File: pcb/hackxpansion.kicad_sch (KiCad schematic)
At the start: 0 parts

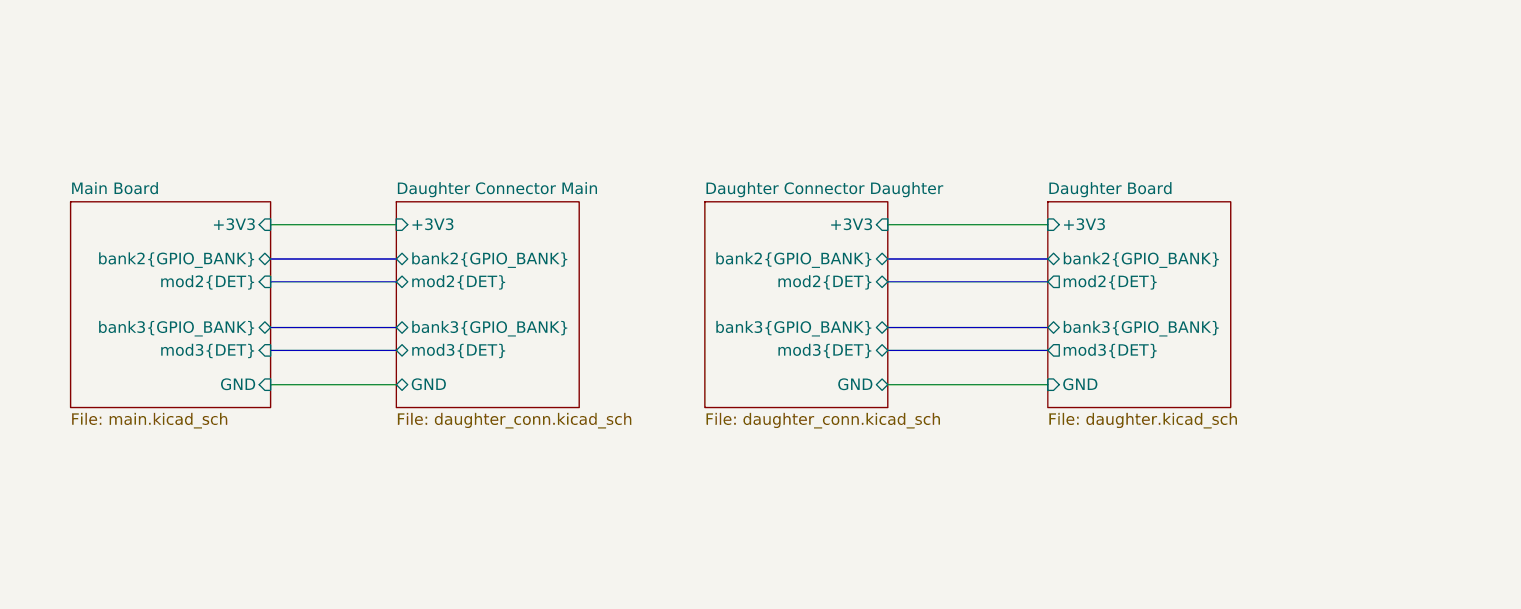
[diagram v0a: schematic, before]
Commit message: finished rough schematic
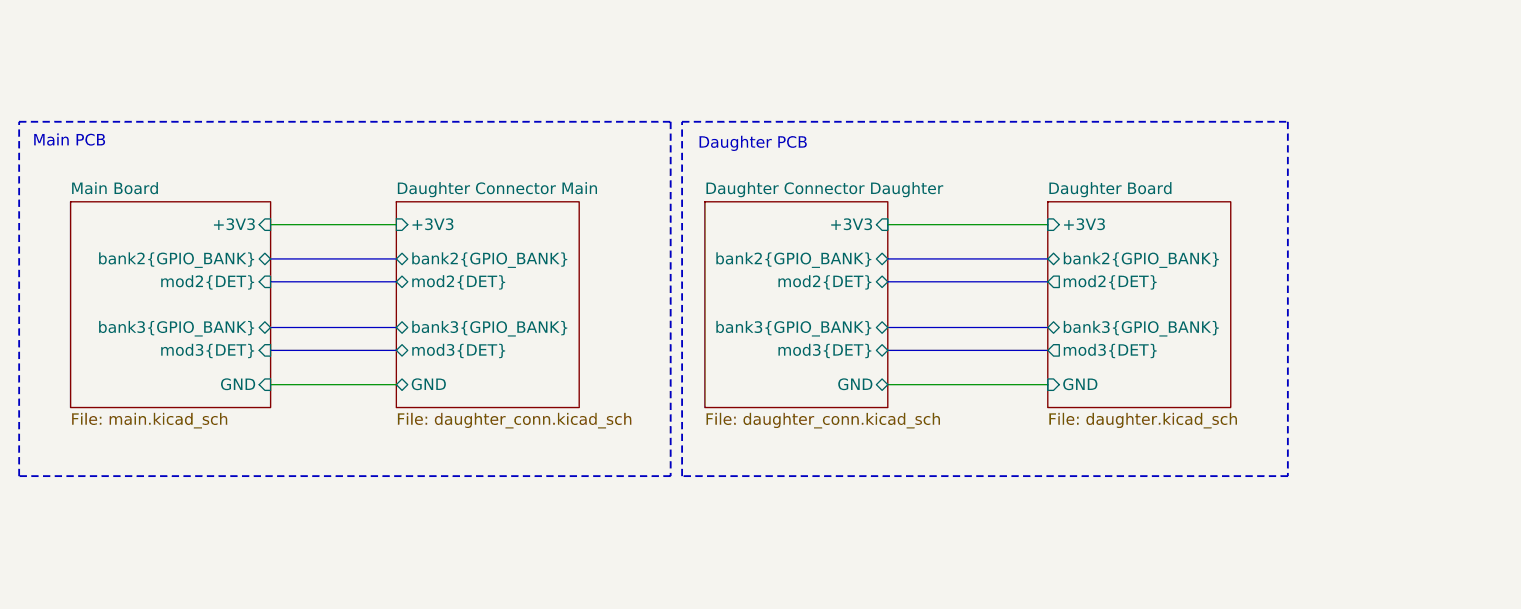
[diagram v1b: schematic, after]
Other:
- note added: "Daughter PCB"
- note added: "Main PCB"
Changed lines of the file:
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@@
 	(generator_version "10.0")
 	(paper "A5")
+	(rectangle
+		(start 26.67 45.72)
+		(end 99.06 85.09)
+		(stroke
+			(width 0.2032)
+			(type dash)
+		)
+		(fill
+			(type none)
+		)
+	)
+	(rectangle
+		(start 100.33 45.72)
+		(end 167.64 85.09)
+		(stroke
+			(width 0.2032)
+			(type dash)
+		)
+		(fill
+			(type none)
+		)
+	)
+	(text "Main PCB"
+		(exclude_from_sim no)
+		(at 32.258 48.006 0)
+		(effects
+			(font
+				(size 1.27 1.27)
+			)
+		)
+	)
+	(text "Daughter PCB"
+		(exclude_from_sim no)
+		(at 108.204 48.26 0)
+		(effects
+			(font
+				(size 1.27 1.27)
+			)
+		)
+	)
 	(bus
 		(pts

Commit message: switched to pico blade connectors
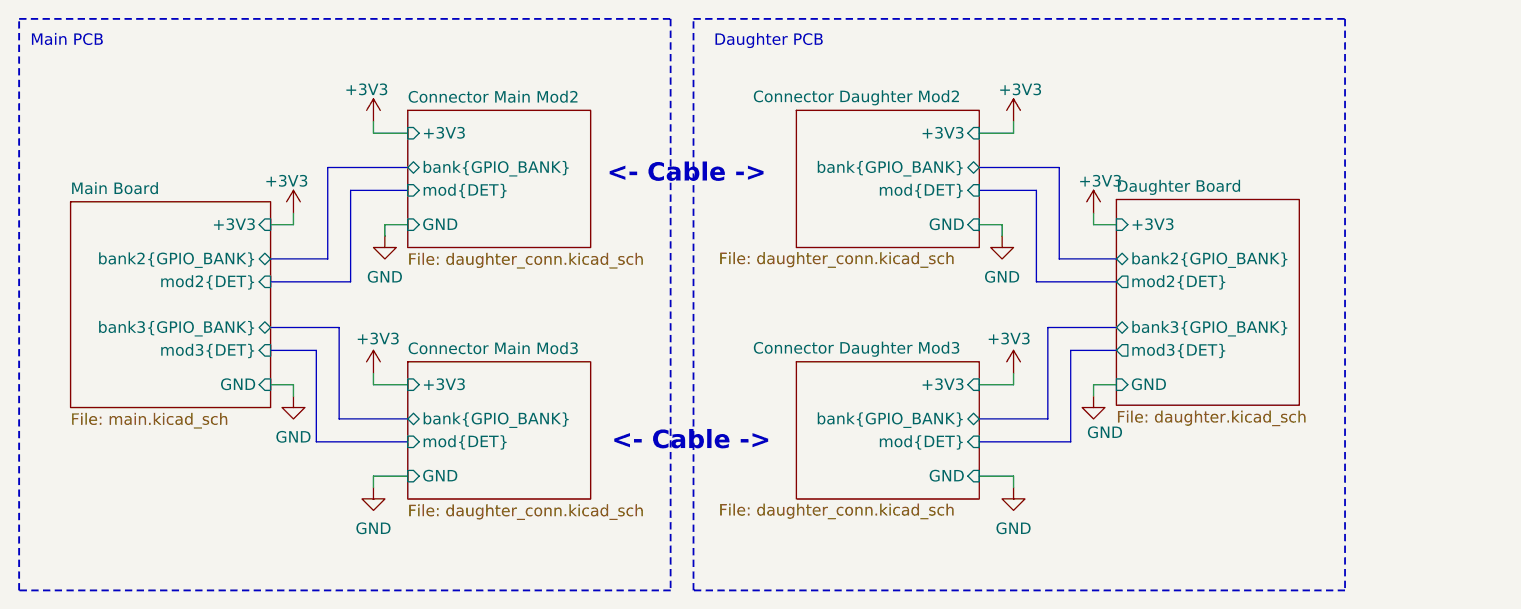
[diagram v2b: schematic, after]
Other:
- sheet Daughter Connector Main renamed Connector Main Mod2
- removed sheet Daughter Connector Daughter
- added sheet Connector Daughter Mod2 (daughter_conn.kicad_sch)
- added sheet Connector Daughter Mod3 (daughter_conn.kicad_sch)
- added sheet Connector Main Mod3 (daughter_conn.kicad_sch)
- sheet Connector Main Mod2 ports: added bank{GPIO_BANK}, mod{DET}; removed bank2{GPIO_BANK}, bank3{GPIO_BANK}, mod2{DET}, mod3{DET}
- note added: "<- Cable ->"

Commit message: moved stuff around
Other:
- note added: "<----Cable---->"
- note removed: "<- Cable ->"

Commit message: worked on routing
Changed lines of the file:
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@@
 	(wire
 		(pts
-			(xy 160.02 55.88) (xy 160.02 57.15)
+			(xy 160.02 52.07) (xy 160.02 57.15)
 		)
 		(stroke
@@
 			)
 		)
-		(property "Value" "+3V3"
+		(property "Value" "DAUGHT_+3V3"
 			(at 150.622 69.85 0)
 			(show_name no)
@@
 			)
 		)
-		(property "Value" "MAIN_GND"
+		(property "Value" "GND"
 			(at 57.15 90.932 0)
 			(show_name no)
@@
 			)
 		)
-		(property "Value" "+3V3"
-			(at 151.892 42.164 0)
+		(property "Value" "DAUGHT_+3V3"
+			(at 160.782 43.942 0)
 			(show_name no)
 			(do_not_autoplace no)
@@
 			)
 		)
-		(property "Value" "MAIN_GND"
+		(property "Value" "GND"
 			(at 67.31 65.532 0)
 			(show_name no)
@@
 		(lib_name "+3V3_1")
 		(lib_id "power:+3V3")
-		(at 160.02 55.88 0)
+		(at 160.02 52.07 0)
 		(mirror y)
 		(unit 1)
@@
 		(dnp no)
 		(property "Reference" "#PWR096"
-			(at 160.02 59.69 0)
-			(hide yes)
-			(show_name no)
-			(do_not_autoplace no)
-			(effects
-				(font
-					(size 1.27 1.27)
-				)
-			)
-		)
-		(property "Value" "+3V3"
-			(at 160.274 52.578 0)
+			(at 160.02 55.88 0)
+			(hide yes)
+			(show_name no)
+			(do_not_autoplace no)
+			(effects
+				(font
+					(size 1.27 1.27)
+				)
+			)
+		)
+		(property "Value" "DAUGHT_+3V3"
+			(at 169.164 50.038 0)
 			(show_name no)
 			(do_not_autoplace no)
@@
 		)
 		(property "Footprint" ""
-			(at 160.02 55.88 0)
+			(at 160.02 52.07 0)
 			(hide yes)
 			(show_name no)
@@
 		)
 		(property "Datasheet" ""
-			(at 160.02 55.88 0)
+			(at 160.02 52.07 0)
 			(hide yes)
 			(show_name no)
@@
 		)
 		(property "Description" "Power symbol creates a global label with name \"+3V3\""
-			(at 160.02 55.88 0)
-			(hide yes)
-			(show_name no)
+			(at 160.02 52.07 0)
+			(hide yes)
+			(show_name no)
